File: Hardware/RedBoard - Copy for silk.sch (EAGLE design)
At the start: 68 parts, among them IC3 LM1117, J1 AMP FCI 10103594-0001LF, J2 ISP, J3 POWER_JACKSUPER_BOMB_DIGITY, Q1 1A/60V/500mΩ, Q2 2N7002PW, Q3 2N7002PW, U1 CH340C, U3 AP2112-3.3V, U4 ATMEGA328P_TQFP, Y1 16MHz

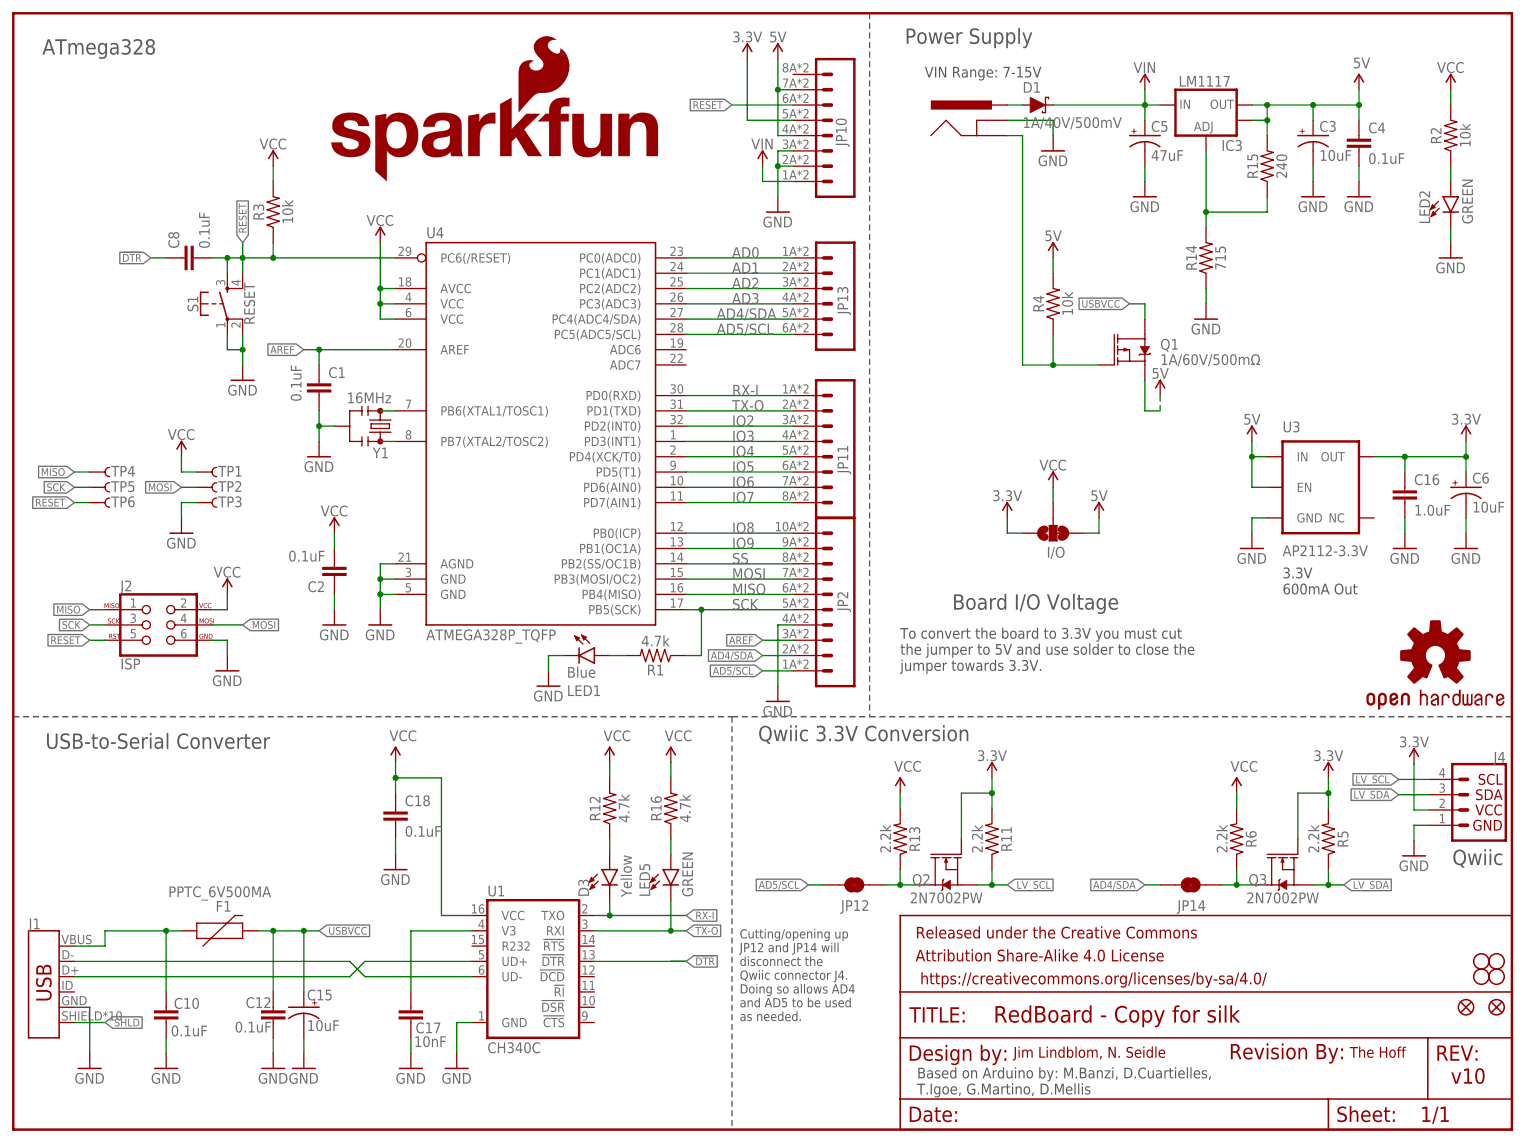
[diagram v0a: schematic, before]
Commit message: Design Review fixes to silk and componenet placement
Design Review fixes to silk and componenet placement
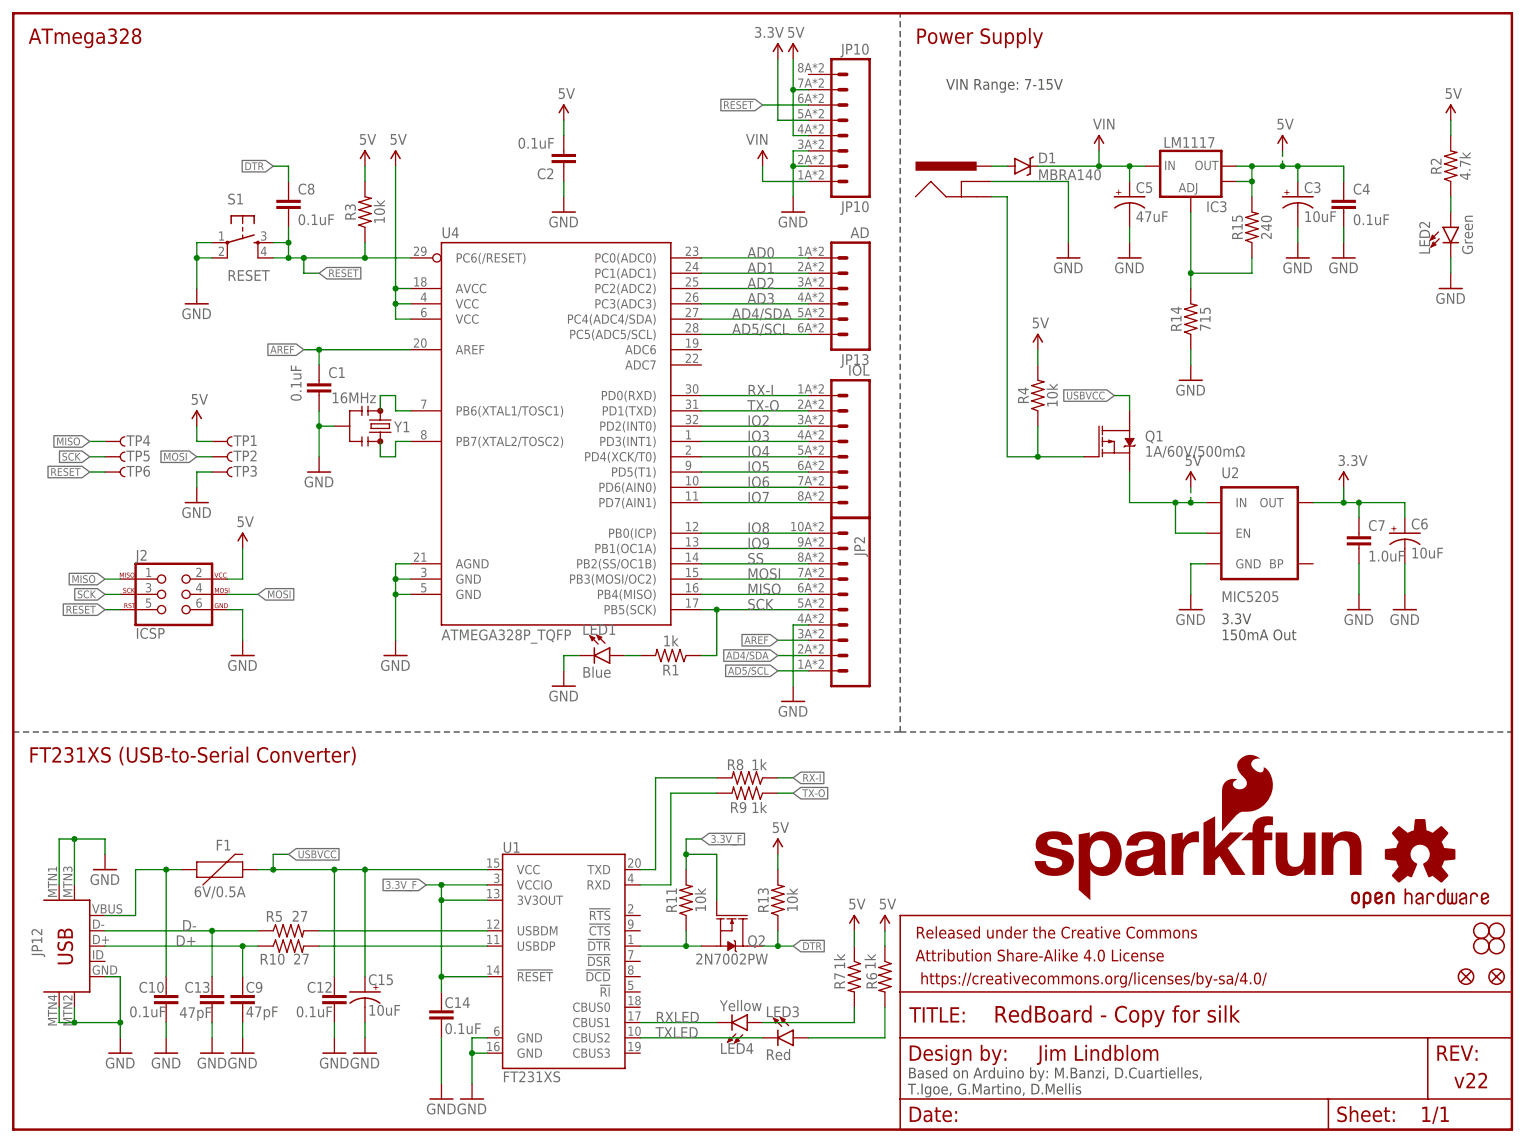
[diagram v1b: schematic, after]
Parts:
- removed C16: 1.0uF, SparkFun-Capacitors:1.0UF-16V-10%(0603)
- removed C17: 10nF, SparkFun-Capacitors:10NF/10000PF-50V-10%(0603)
- removed C18: 0.1uF, SparkFun-Capacitors:0.1UF-25V(+80/-20%)(0603)
- removed D3: Yellow, SparkFun-LED:LED-YELLOW_HIDDENSILK
- removed I/O: JUMPER-SMT_3_1-NC_TRACE_SILK, SparkFun-Jumpers:JUMPER-SMT_3_1-NC_TRACE_SILK
- removed J1: AMP FCI 10103594-0001LF, SparkFun-Connectors:USB_MICRO-B_HALF_PTH_MILL
- removed J4: (no value), SparkFun-Connectors:QWIIC_CONNECTORJS-1MM
- removed JP14: JUMPER-SMT_2_NC_TRACE_SILK, SparkFun-Jumpers:JUMPER-SMT_2_NC_TRACE_SILK
- removed LED5: GREEN, SparkFun-LED:LED-GREEN_HIDDENSILK
- removed LOGO1: REVISION, SparkFun-Aesthetics:REVISION
- removed Q3: 2N7002PW, SparkFun-DiscreteSemi:MOSFET-NCH-2N7002PW
- removed R12, R16: 4.7k, SparkFun-Resistors:4.7KOHM-0603-1/10W-1%
- removed U3: AP2112-3.3V, SparkFun-PowerIC:V_REG_AP2112K-3.3V
- added C13, C9: 47pF, SparkFun-Capacitors:47PF-0603-50V-5%
- added C14: 0.1uF, SparkFun-Capacitors:0.1UF-0603-25V-(+80/-20%)
- added C7: 1.0uF, SparkFun-Capacitors:1.0UF-0603-16V-10%
- added LED3: Red, SparkFun-LED:LED1206
- added LED4: Yellow, SparkFun-LED:LED1206
- added R10: 27, SparkFun-Resistors:27OHM-0603-1/10W-1%
- added R7, R8, R9: 1k, SparkFun-Resistors:1KOHM-0603-1/10W-1%
- added U2: MIC5205, SparkFun-PowerIC:MIC52053.3V
- D1: value 1A/40V/500mV -> MBRA140; device SparkFun-DiscreteSemi:DIODE-SCHOTTKY-SS14 -> SparkFun-DiscreteSemi:MBRA140
- F1: value PPTC_6V500MA -> 6V/0.5A; device SparkFun-Fuses:PPTC_6V500MA -> SparkFun-Fuses:PTC-HALF_AMP
- J2: value ISP -> ICSP
- JP10: value (none) -> JP10
- JP11: value JP11 -> IOL
- JP12: value JUMPER-SMT_2_NC_TRACE_SILK -> USB-MINIB-5PIN; device SparkFun-Jumpers:JUMPER-SMT_2_NC_TRACE_SILK -> SparkFun-Connectors:USB-MINIB-5PIN
- JP13: value (none) -> AD
- LED1: device SparkFun-LED:LED-BLUE_HIDDENSILK -> SparkFun-LED:LED1206
- LED2: value GREEN -> Green; device SparkFun-LED:LED-GREEN_HIDDENSILK -> SparkFun-LED:LED1206
- R1: value 4.7k -> 1k; device SparkFun-Resistors:4.7KOHM-0603-1/10W-1% -> SparkFun-Resistors:1KOHM-0603-1/10W-1%
- R11, R13: value 2.2k -> 10k; device SparkFun-Resistors:2.2KOHM-0603-1/10W-1% -> SparkFun-Resistors:10KOHM-0603-1/10W-1%
- R2: value 10k -> 4.7k; device SparkFun-Resistors:10KOHM-0603-1/10W-1% -> SparkFun-Resistors:4.7KOHM-0603-1/10W-1%
- R5: value 2.2k -> 27; device SparkFun-Resistors:2.2KOHM-0603-1/10W-1% -> SparkFun-Resistors:27OHM-0603-1/10W-1%
- R6: value 2.2k -> 1k; device SparkFun-Resistors:2.2KOHM-0603-1/10W-1% -> SparkFun-Resistors:1KOHM-0603-1/10W-1%
- S1: device SparkFun-Switches:MOMENTARY-SWITCH-SPST-2-SMD-5.2MM-TALL -> SparkFun-Electromechanical:SWITCH_SPST_4_PINSQUARE
- U1: value CH340C -> FT231XS; device SparkFun-IC-Comms:CH340C -> SparkFun-IC-Comms:FT231XS
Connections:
- removed net !DTR: C8.1, U1.!DTR
- removed net LV_SCL: J4.4, Q2.S, R11.1
- removed net LV_SDA: J4.3, Q3.S, R5.1
- removed net N$13: J1.D-, U1.UD-
- removed net N$14: J1.D+, U1.UD+
- removed net N$5: LED5.A, R16.1
- removed net N$9: D3.A, R12.1
- removed net SHLD: J1.SHIELD
- removed net VCC: C18.1, C2.2, I/O.2, J2.2, R12.2, R13.2, R16.2, R2.2, R3.2, R6.2, TP1.1, U1.VCC, U4.AVCC, U4.VCC@4, U4.VCC@6
- new net 3.3V_F: C14.1, Q2.G, R11.2, U1.!RESET, U1.3V3OUT, U1.VCCIO
- new net D+: C9.1, JP12.D+, R10.1
- new net D-: C13.1, JP12.D-, R5.1
- new net DTR: C8.1, Q2.D, R13.1
- new net FTDI_DTR: Q2.S, R11.1, U1.!DTR
- new net N$10: LED4.A, R7.2
- new net RXD: R9.2, U1.RXD
- new net RXLED: LED4.C, U1.CBUS1
- new net TXD: R8.2, U1.TXD
- new net TXLED: LED3.C, U1.CBUS2
- net 3.3V: now also C7.1, U2.OUT; no longer C16.1, I/O.1, J4.2, Q2.G, Q3.G, R11.2, R5.2, U3.OUT
- net 5V: now also C2.2, J2.2, R13.2, R2.2, R3.2, R6.1, R7.1, TP1.1, U2.EN, U2.IN, U4.AVCC, U4.VCC@4, U4.VCC@6; no longer I/O.3, U3.EN, U3.IN
- net AD4/SDA: no longer JP14.2
- net AD5/SCL: no longer JP12.2
- net GND: now also C13.2, C14.2, C7.2, C9.2, JP12.GND, JP12.MTN1, JP12.MTN2, JP12.MTN3, JP12.MTN4, U1.GND@16, U1.GND@6, U2.GND; no longer C16.2, C17.2, C18.2, J1.GND, J4.1, U1.GND, U3.GND
- net N$6: now also R5.2, U1.USBDM; no longer C17.1, U1.V3
- net N$7: now also R10.2, U1.USBDP; no longer JP12.1, Q2.D, R13.1
- net N$8: now also LED3.A, R6.2; no longer JP14.1, Q3.D, R6.1
- net RX-I: now also R8.1; no longer D3.C, U1.TXO
- net TX-O: now also R9.1; no longer LED5.C, U1.RXI
- net USBVCC: now also U1.VCC
- net VUSB: now also JP12.VBUS; no longer J1.VBUS
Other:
- note added: "3.3V 150mA Out"
- note added: "FT231XS (USB-to-Serial Converter)"
- note added: "Jim Lindblom"
- note added: "v22"
- note removed: "3.3V 600mA Out"
- note removed: "Board I/O Voltage"
- note removed: "Cutting/opening up JP12 and JP14 will disconnect the Qwiic connector J4. Doing so allows AD4 and AD5 to be used as needed."
- note removed: "Jim Lindblom, N. Seidle"
- note removed: "Qwiic"
- note removed: "Qwiic 3.3V Conversion"
- note removed: "The Hoff"
- note removed: "To convert the board to 3.3V you must cut the jumper to 5V and use solder to close the jumper towards 3.3V."
- note removed: "USB-to-Serial Converter"
- note removed: "v10"
- moved on the sheet: C10, C12, C15, C2, C3, C4, C5, C6, C8, IC3, J2, JP10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
